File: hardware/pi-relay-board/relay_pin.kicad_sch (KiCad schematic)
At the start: 4 parts, among them J3 Conn_01x03_Socket, K2 TIANBO-HJR-4102-L, Q11 BC847

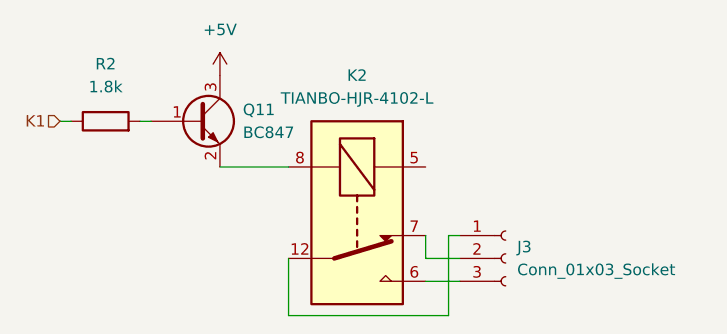
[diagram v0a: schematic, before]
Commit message: hardware: change to tht
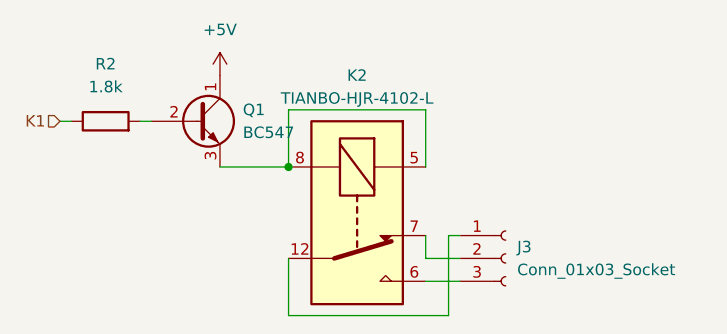
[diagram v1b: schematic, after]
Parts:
- removed Q11: BC847, Package_TO_SOT_SMD:SOT-23, symbol Transistor_BJT:BC847
- added Q1: BC547, Package_TO_SOT_THT:TO-92_Inline, symbol Transistor_BJT:BC547
- R2: footprint Resistor_SMD:R_0805_2012Metric_Pad1.20x1.40mm_HandSolder -> Resistor_THT:R_Axial_DIN0207_L6.3mm_D2.5mm_P7.62mm_Horizontal
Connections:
- net +5V: now also Q1.1 (C)
- net at R2.2: now also Q1.2 (B)
- net at K2.5: now also K2.8, Q1.3 (E)
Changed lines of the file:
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@@
 	(generator_version "8.0")
 	(paper "A4")
+	(junction
+		(at 120.65 73.66)
+		(diameter 0)
+		(color 0 0 0 0)
+	)
+	(wire
+		(pts
+			(xy 120.65 67.31) (xy 120.65 73.66)
+		)
+		(stroke
+			(width 0)
+			(type default)
+		)
+	)
 	(wire
 		(pts
@@
 	(wire
 		(pts
+			(xy 135.89 73.66) (xy 135.89 67.31)
+		)
+		(stroke
+			(width 0)
+			(type default)
+		)
+	)
+	(wire
+		(pts
 			(xy 135.89 81.28) (xy 135.89 83.82)
 		)
@@
 		(pts
 			(xy 120.65 83.82) (xy 120.65 90.17)
+		)
+		(stroke
+			(width 0)
+			(type default)
+		)
+	)
+	(wire
+		(pts
+			(xy 135.89 67.31) (xy 120.65 67.31)
 		)
 		(stroke
@@
 			)
 			(justify right)
+		)
+	)
+	(symbol
+		(lib_id "Transistor_BJT:BC547")
+		(at 110.49 68.58 0)
+		(unit 1)
+		(exclude_from_sim no)
+		(in_bom yes)
+		(on_board yes)
+		(dnp no)
+		(fields_autoplaced yes)
+		(property "Reference" "Q1"
+			(at 115.57 67.3099 0)
+			(effects
+				(font
+					(size 1.27 1.27)
+				)
+				(justify left)
+			)
+		)
+		(property "Value" "BC547"
+			(at 115.57 69.8499 0)
+			(effects
+				(font
+					(size 1.27 1.27)
+				)
+				(justify left)
+			)
+		)
+		(property "Footprint" "Package_TO_SOT_THT:TO-92_Inline"
+			(at 115.57 70.485 0)
+			(effects
+				(font
+					(size 1.27 1.27)
+					(italic yes)
+				)
+				(justify left)
+				(hide yes)
+			)
+		)
+		(property "Datasheet" "https://www.onsemi.com/pub/Collateral/BC550-D.pdf"
+			(at 110.49 68.58 0)
+			(effects
+				(font
+					(size 1.27 1.27)
+				)
+				(justify left)
+				(hide yes)
+			)
+		)
+		(property "Description" "0.1A Ic, 45V Vce, Small Signal NPN Transistor, TO-92"
+			(at 110.49 68.58 0)
+			(effects
+				(font
+					(size 1.27 1.27)
+				)
+				(hide yes)
+			)
+		)
+		(pin "3"
+		)
+		(pin "1"
+		)
+		(pin "2"
+		)
+		(instances
+			(project "pi-relay-board"
+				(path "/d2fef91f-5840-4773-b01e-415a95bac3ff/691f66ce-a9a7-4210-8330-e484efbc945d"
+					(reference "Q1")
+					(unit 1)
+				)
+				(path "/d2fef91f-5840-4773-b01e-415a95bac3ff/e003dbba-e903-4928-939e-ed45384c32ae"
+					(reference "Q2")
+					(unit 1)
+				)
+				(path "/d2fef91f-5840-4773-b01e-415a95bac3ff/4104c2a8-b10b-4814-8630-4176455720ff"
+					(reference "Q3")
+					(unit 1)
+				)
+				(path "/d2fef91f-5840-4773-b01e-415a95bac3ff/4160e499-e228-48ff-bf19-fbbc4f79d536"
+					(reference "Q4")
+					(unit 1)
+				)
+				(path "/d2fef91f-5840-4773-b01e-415a95bac3ff/57158c3d-53e9-4aea-9df5-f221bf193187"
+					(reference "Q5")
+					(unit 1)
+				)
+				(path "/d2fef91f-5840-4773-b01e-415a95bac3ff/1516f555-b572-405c-8e26-5409c4128995"
+					(reference "Q6")
+					(unit 1)
+				)
+				(path "/d2fef91f-5840-4773-b01e-415a95bac3ff/118fbb03-b0f5-4e81-9827-73e518015949"
+					(reference "Q7")
+					(unit 1)
+				)
+				(path "/d2fef91f-5840-4773-b01e-415a95bac3ff/a3c9cc38-888b-4558-9948-ff007dba1d89"
+					(reference "Q8")
+					(unit 1)
+				)
+				(path "/d2fef91f-5840-4773-b01e-415a95bac3ff/85065515-af0d-46e8-9ec7-79bcf82b83a9"
+					(reference "Q9")
+					(unit 1)
+				)
+				(path "/d2fef91f-5840-4773-b01e-415a95bac3ff/e35df33e-9fd4-4492-8686-e97c7371f93f"
+					(reference "Q10")
+					(unit 1)
+				)
+			)
 		)
 	)
@@
 			)
 		)
-		(property "Footprint" "Resistor_SMD:R_0805_2012Metric_Pad1.20x1.40mm_HandSolder"
+		(property "Footprint" "Resistor_THT:R_Axial_DIN0207_L6.3mm_D2.5mm_P7.62mm_Horizontal"
 			(at 100.33 70.358 90)
 			(effects
@@
 					(unit 1)
 				)
-			)
-		)
-	)
-	(symbol
-		(lib_id "Transistor_BJT:BC847")
-		(at 110.49 68.58 0)
-		(unit 1)
-		(exclude_from_sim no)
-		(in_bom yes)
-		(on_board yes)
-		(dnp no)
-		(fields_autoplaced yes)
-		(property "Reference" "Q11"
-			(at 115.57 67.3099 0)
-			(effects
-				(font
-					(size 1.27 1.27)
-				)
-				(justify left)
-			)
-		)
-		(property "Value" "BC847"
-			(at 115.57 69.8499 0)
-			(effects
-				(font
-					(size 1.27 1.27)
-				)
-				(justify left)
-			)
-		)
-		(property "Footprint" "Package_TO_SOT_SMD:SOT-23"
-			(at 115.57 70.485 0)
-			(effects
-				(font
-					(size 1.27 1.27)
-					(italic yes)
-				)
-				(justify left)
-				(hide yes)
-			)
-		)
-		(property "Datasheet" "http://www.infineon.com/dgdl/Infineon-BC847SERIES_BC848SERIES_BC849SERIES_BC850SERIES-DS-v01_01-en.pdf?fileId=db3a304314dca389011541d4630a1657"
-			(at 110.49 68.58 0)
-			(effects
-				(font
-					(size 1.27 1.27)
-				)
-				(justify left)
-				(hide yes)
-			)
-		)
-		(property "Description" "0.1A Ic, 45V Vce, NPN Transistor, SOT-23"
-			(at 110.49 68.58 0)
-			(effects
-				(font
-					(size 1.27 1.27)
-				)
-				(hide yes)
-			)
-		)
-		(pin "3"
-		)
-		(pin "2"
-		)
-		(pin "1"
-		)
-		(instances
-			(project "pi-relay-board"
-				(path "/d2fef91f-5840-4773-b01e-415a95bac3ff/691f66ce-a9a7-4210-8330-e484efbc945d"
-					(reference "Q11")
-					(unit 1)
-				)
-				(path "/d2fef91f-5840-4773-b01e-415a95bac3ff/e003dbba-e903-4928-939e-ed45384c32ae"
-					(reference "Q12")
-					(unit 1)
-				)
-				(path "/d2fef91f-5840-4773-b01e-415a95bac3ff/4104c2a8-b10b-4814-8630-4176455720ff"
-					(reference "Q13")
-					(unit 1)
-				)
-				(path "/d2fef91f-5840-4773-b01e-415a95bac3ff/4160e499-e228-48ff-bf19-fbbc4f79d536"
-					(reference "Q14")
-					(unit 1)
-				)
-				(path "/d2fef91f-5840-4773-b01e-415a95bac3ff/57158c3d-53e9-4aea-9df5-f221bf193187"
-					(reference "Q15")
-					(unit 1)
-				)
-				(path "/d2fef91f-5840-4773-b01e-415a95bac3ff/1516f555-b572-405c-8e26-5409c4128995"
-					(reference "Q16")
-					(unit 1)
-				)
-				(path "/d2fef91f-5840-4773-b01e-415a95bac3ff/118fbb03-b0f5-4e81-9827-73e518015949"
-					(reference "Q17")
-					(unit 1)
-				)
-				(path "/d2fef91f-5840-4773-b01e-415a95bac3ff/a3c9cc38-888b-4558-9948-ff007dba1d89"
-					(reference "Q18")
-					(unit 1)
-				)
-				(path "/d2fef91f-5840-4773-b01e-415a95bac3ff/85065515-af0d-46e8-9ec7-79bcf82b83a9"
-					(reference "Q19")
-					(unit 1)
-				)
-				(path "/d2fef91f-5840-4773-b01e-415a95bac3ff/e35df33e-9fd4-4492-8686-e97c7371f93f"
-					(reference "Q20")
-					(unit 1)
-				)

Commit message: feat: pcb bc547 footprint, laser image
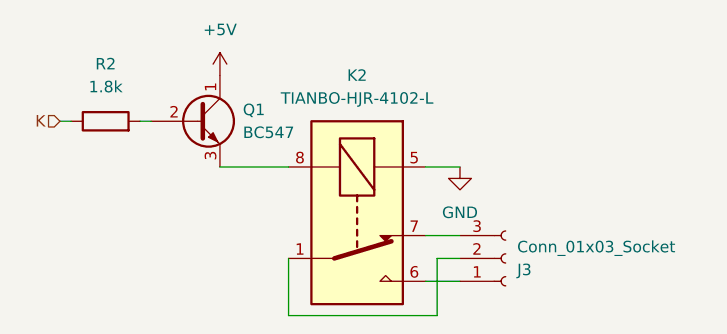
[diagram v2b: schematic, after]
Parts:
- Q1: footprint Package_TO_SOT_THT:TO-92_Inline -> Package_TO_SOT_THT:TO-92_HandSolder
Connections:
- net at K2.8, Q1.3 (E): no longer K2.5
- net at J3.1 (Pin_1): now also K2.6; no longer K2.12
- net at J3.3 (Pin_3): now also K2.7; no longer K2.6
- net at J3.2 (Pin_2): now also K2.1; no longer K2.7
- net K1 renamed K
- new net GND: K2.5
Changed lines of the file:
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@@
 	(generator_version "8.0")
 	(paper "A4")
-	(junction
-		(at 120.65 73.66)
-		(diameter 0)
-		(color 0 0 0 0)
-	)
-	(wire
-		(pts
-			(xy 120.65 67.31) (xy 120.65 73.66)
-		)
-		(stroke
-			(width 0)
-			(type default)
-		)
-	)
-	(wire
-		(pts
-			(xy 135.89 83.82) (xy 139.7 83.82)
+	(wire
+		(pts
+			(xy 137.16 83.82) (xy 139.7 83.82)
 		)
 		(stroke
@@
 	(wire
 		(pts
-			(xy 135.89 73.66) (xy 135.89 67.31)
-		)
-		(stroke
-			(width 0)
-			(type default)
-		)
-	)
-	(wire
-		(pts
-			(xy 135.89 81.28) (xy 135.89 83.82)
-		)
-		(stroke
-			(width 0)
-			(type default)
-		)
-	)
-	(wire
-		(pts
-			(xy 120.65 90.17) (xy 138.43 90.17)
-		)
-		(stroke
-			(width 0)
-			(type default)
-		)
-	)
-	(wire
-		(pts
-			(xy 138.43 90.17) (xy 138.43 81.28)
+			(xy 137.16 90.17) (xy 137.16 83.82)
+		)
+		(stroke
+			(width 0)
+			(type default)
+		)
+	)
+	(wire
+		(pts
+			(xy 139.7 73.66) (xy 135.89 73.66)
+		)
+		(stroke
+			(width 0)
+			(type default)
+		)
+	)
+	(wire
+		(pts
+			(xy 135.89 81.28) (xy 139.7 81.28)
+		)
+		(stroke
+			(width 0)
+			(type default)
+		)
+	)
+	(wire
+		(pts
+			(xy 120.65 90.17) (xy 137.16 90.17)
 		)
 		(stroke
@@
 	(wire
 		(pts
-			(xy 138.43 81.28) (xy 139.7 81.28)
-		)
-		(stroke
-			(width 0)
-			(type default)
-		)
-	)
-	(wire
-		(pts
 			(xy 104.14 68.58) (xy 105.41 68.58)
 		)
@@
 		)
 	)
-	(wire
-		(pts
-			(xy 135.89 67.31) (xy 120.65 67.31)
-		)
-		(stroke
-			(width 0)
-			(type default)
-		)
-	)
-	(hierarchical_label "K1"
+	(hierarchical_label "K"
 		(shape input)
 		(at 95.25 68.58 180)
@@
 			)
 		)
-		(property "Footprint" "Package_TO_SOT_THT:TO-92_Inline"
+		(property "Footprint" "Package_TO_SOT_THT:TO-92_HandSolder"
 			(at 115.57 70.485 0)
 			(effects
@@
 		(pin "5"
 		)
-		(pin "12"
+		(pin "1"
 		)
 		(pin "6"
@@
 		(lib_id "Connector:Conn_01x03_Socket")
 		(at 144.78 83.82 0)
+		(mirror x)
+		(unit 1)
+		(exclude_from_sim no)
+		(in_bom yes)
+		(on_board yes)
+		(dnp no)
+		(property "Reference" "J3"
+			(at 146.05 85.0901 0)
+			(effects
+				(font
+					(size 1.27 1.27)
+				)
+				(justify left)
+			)
+		)
+		(property "Value" "Conn_01x03_Socket"
+			(at 146.05 82.5501 0)
+			(effects
+				(font
+					(size 1.27 1.27)
+				)
+				(justify left)
+			)
+		)
+		(property "Footprint" "TerminalBlock_Phoenix:TerminalBlock_Phoenix_PT-1,5-3-3.5-H_1x03_P3.50mm_Horizontal"
+			(at 144.78 83.82 0)
+			(effects
+				(font
+					(size 1.27 1.27)
+				)
+				(hide yes)
+			)
+		)
+		(property "Datasheet" "~"
+			(at 144.78 83.82 0)
+			(effects
+				(font
+					(size 1.27 1.27)
+				)
+				(hide yes)
+			)
+		)
+		(property "Description" "Generic connector, single row, 01x03, script generated"
+			(at 144.78 83.82 0)
+			(effects
+				(font
+					(size 1.27 1.27)
+				)
+				(hide yes)
+			)
+		)
+		(pin "1"
+		)
+		(pin "2"
+		)
+		(pin "3"
+		)
+		(instances
+			(project "pi-relay-board"
+				(path "/d2fef91f-5840-4773-b01e-415a95bac3ff/691f66ce-a9a7-4210-8330-e484efbc945d"
+					(reference "J3")
+					(unit 1)
+				)
+				(path "/d2fef91f-5840-4773-b01e-415a95bac3ff/e003dbba-e903-4928-939e-ed45384c32ae"
+					(reference "J2")
+					(unit 1)
+				)
+				(path "/d2fef91f-5840-4773-b01e-415a95bac3ff/4104c2a8-b10b-4814-8630-4176455720ff"
+					(reference "J4")
+					(unit 1)
+				)
+				(path "/d2fef91f-5840-4773-b01e-415a95bac3ff/4160e499-e228-48ff-bf19-fbbc4f79d536"
+					(reference "J5")
+					(unit 1)
+				)
+				(path "/d2fef91f-5840-4773-b01e-415a95bac3ff/57158c3d-53e9-4aea-9df5-f221bf193187"
+					(reference "J6")
+					(unit 1)
+				)
+				(path "/d2fef91f-5840-4773-b01e-415a95bac3ff/1516f555-b572-405c-8e26-5409c4128995"
+					(reference "J7")
+					(unit 1)
+				)
+				(path "/d2fef91f-5840-4773-b01e-415a95bac3ff/118fbb03-b0f5-4e81-9827-73e518015949"
+					(reference "J8")
+					(unit 1)
+				)
+				(path "/d2fef91f-5840-4773-b01e-415a95bac3ff/a3c9cc38-888b-4558-9948-ff007dba1d89"
+					(reference "J9")
+					(unit 1)
+				)
+				(path "/d2fef91f-5840-4773-b01e-415a95bac3ff/85065515-af0d-46e8-9ec7-79bcf82b83a9"
+					(reference "J10")
+					(unit 1)
+				)
+				(path "/d2fef91f-5840-4773-b01e-415a95bac3ff/e35df33e-9fd4-4492-8686-e97c7371f93f"
+					(reference "J11")
+					(unit 1)
+				)
+			)
+		)
+	)
+	(symbol
+		(lib_id "power:GND")
+		(at 139.7 73.66 0)
 		(unit 1)
 		(exclude_from_sim no)
@@
 		(dnp no)
 		(fields_autoplaced yes)
-		(property "Reference" "J3"
-			(at 146.05 82.5499 0)
-			(effects
-				(font
-					(size 1.27 1.27)
-				)
-				(justify left)
-			)
-		)
-		(property "Value" "Conn_01x03_Socket"
-			(at 146.05 85.0899 0)
-			(effects
-				(font
-					(size 1.27 1.27)
-				)
-				(justify left)
-			)
-		)
-		(property "Footprint" "TerminalBlock_Phoenix:TerminalBlock_Phoenix_PT-1,5-3-3.5-H_1x03_P3.50mm_Horizontal"
-			(at 144.78 83.82 0)
-			(effects
-				(font
-					(size 1.27 1.27)
-				)
-				(hide yes)
-			)
-		)
-		(property "Datasheet" "~"
-			(at 144.78 83.82 0)
-			(effects
-				(font
-					(size 1.27 1.27)
-				)
-				(hide yes)
-			)
-		)
-		(property "Description" "Generic connector, single row, 01x03, script generated"
-			(at 144.78 83.82 0)
+		(property "Reference" "#PWR019"
+			(at 139.7 80.01 0)
+			(effects
+				(font
+					(size 1.27 1.27)
+				)
+				(hide yes)
+			)
+		)
+		(property "Value" "GND"
+			(at 139.7 78.74 0)
+			(effects
+				(font
+					(size 1.27 1.27)
+				)
+			)
+		)
+		(property "Footprint" ""
+			(at 139.7 73.66 0)
+			(effects
+				(font
+					(size 1.27 1.27)
+				)
+				(hide yes)
+			)
+		)
+		(property "Datasheet" ""
+			(at 139.7 73.66 0)
+			(effects
+				(font
+					(size 1.27 1.27)
+				)
+				(hide yes)
+			)
+		)
+		(property "Description" "Power symbol creates a global label with name \"GND\" , ground"
+			(at 139.7 73.66 0)
 			(effects
 				(font
@@
 		)
 		(pin "1"
-		)
-		(pin "2"
-		)
-		(pin "3"
 		)
 		(instances
 			(project "pi-relay-board"
+				(path "/d2fef91f-5840-4773-b01e-415a95bac3ff/1516f555-b572-405c-8e26-5409c4128995"
+					(reference "#PWR019")
+					(unit 1)
+				)
 				(path "/d2fef91f-5840-4773-b01e-415a95bac3ff/691f66ce-a9a7-4210-8330-e484efbc945d"
-					(reference "J3")
+					(reference "#PWR014")
 					(unit 1)
 				)
 				(path "/d2fef91f-5840-4773-b01e-415a95bac3ff/e003dbba-e903-4928-939e-ed45384c32ae"
-					(reference "J2")
+					(reference "#PWR015")
 					(unit 1)
 				)
 				(path "/d2fef91f-5840-4773-b01e-415a95bac3ff/4104c2a8-b10b-4814-8630-4176455720ff"
-					(reference "J4")
+					(reference "#PWR016")
 					(unit 1)
 				)
 				(path "/d2fef91f-5840-4773-b01e-415a95bac3ff/4160e499-e228-48ff-bf19-fbbc4f79d536"
-					(reference "J5")
+					(reference "#PWR017")
 					(unit 1)
 				)
 				(path "/d2fef91f-5840-4773-b01e-415a95bac3ff/57158c3d-53e9-4aea-9df5-f221bf193187"
-					(reference "J6")
-					(unit 1)
-				)
-				(path "/d2fef91f-5840-4773-b01e-415a95bac3ff/1516f555-b572-405c-8e26-5409c4128995"
-					(reference "J7")
+					(reference "#PWR018")
 					(unit 1)
 				)
 				(path "/d2fef91f-5840-4773-b01e-415a95bac3ff/118fbb03-b0f5-4e81-9827-73e518015949"
-					(reference "J8")
+					(reference "#PWR020")
 					(unit 1)
 				)
 				(path "/d2fef91f-5840-4773-b01e-415a95bac3ff/a3c9cc38-888b-4558-9948-ff007dba1d89"
-					(reference "J9")
+					(reference "#PWR021")
 					(unit 1)
 				)
 				(path "/d2fef91f-5840-4773-b01e-415a95bac3ff/85065515-af0d-46e8-9ec7-79bcf82b83a9"
-					(reference "J10")
+					(reference "#PWR022")
 					(unit 1)
 				)
 				(path "/d2fef91f-5840-4773-b01e-415a95bac3ff/e35df33e-9fd4-4492-8686-e97c7371f93f"
-					(reference "J11")
-					(unit 1)
-				)
+					(reference "#PWR023")
+					(unit 1)
+				)
